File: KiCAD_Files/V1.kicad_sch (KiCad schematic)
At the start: 33 parts, among them SW1 SW_Push, SW2 SW_Push, SW3 SW_Push, U1 NodeMCU_1.0_(ESP-12E), U2 LM35-LP

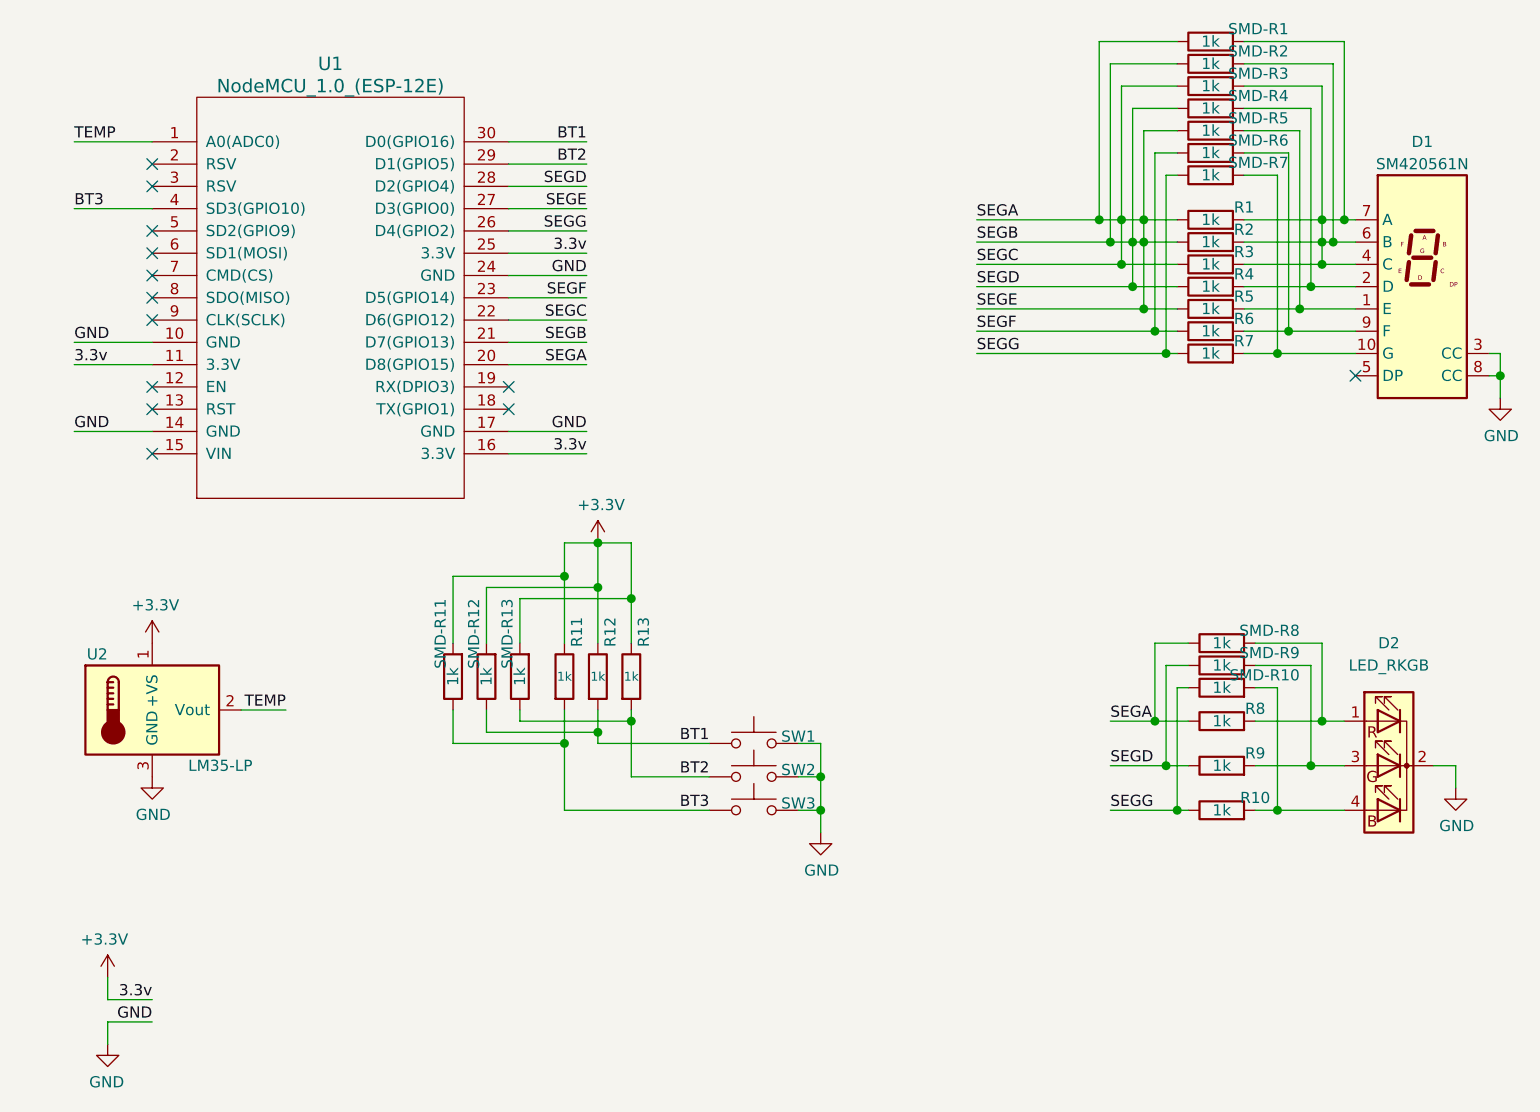
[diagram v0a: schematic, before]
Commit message: Updated Schematic. Started a Getting Started guide
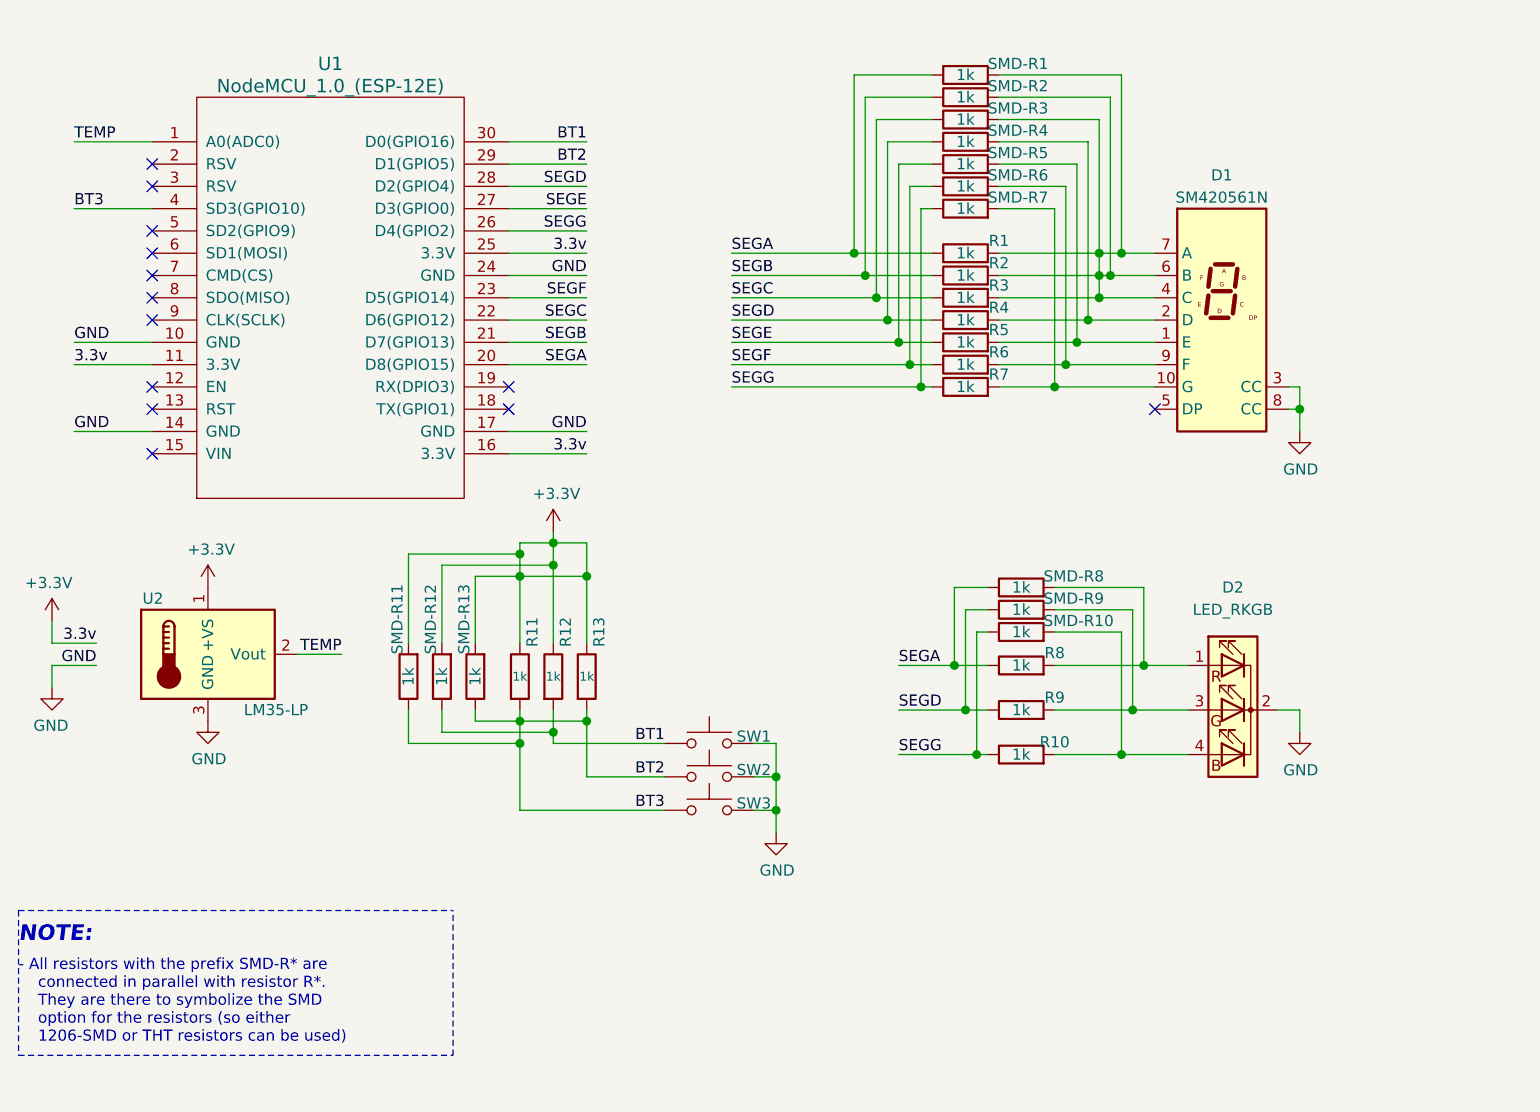
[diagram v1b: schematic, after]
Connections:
- net BT3 is gone; now on net BT2: R11.2, SMD-R11.1, SW3.1, U1.4 (SD3(GPIO10))
- net SEGA: no longer R2.1, R3.1, R4.1, R5.1, R9.1, SMD-R2.1, SMD-R3.1, SMD-R4.1, SMD-R5.1, SMD-R9.1, U1.21 (D7(GPIO13)), U1.22 (D6(GPIO12)), U1.27 (D3(GPIO0)), U1.28 (D2(GPIO4))
- new net SEGB: R2.1, SMD-R2.1, U1.21 (D7(GPIO13))
- new net SEGC: R3.1, SMD-R3.1, U1.22 (D6(GPIO12))
- new net SEGD: R4.1, R9.1, SMD-R4.1, SMD-R9.1, U1.28 (D2(GPIO4))
- new net SEGE: R5.1, SMD-R5.1, U1.27 (D3(GPIO0))
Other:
- note added: "- All resistors with the prefix SMD-R* are connected in parallel with resistor R*. They are there to symbolize the SMD option for the resistors (so either 1206-SMD or THT resistors can be used)"
- note added: "NOTE:"
- company: UNewHaven -> Electro707
- moved on the sheet: D1, D2, R1, R10, R11, R12, R13, R2, R3, R4, R5, R6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

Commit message: Added .net file. Changed origin. Last commit for V1 PCB
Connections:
- net BT2: no longer R11.2, SMD-R11.1, SW3.1, U1.4 (SD3(GPIO10))
- new net: D1.4 (C), R3.2, SMD-R3.2
- new net: D1.6 (B), R2.2, SMD-R2.2
- new net: D1.7 (A), R1.2, SMD-R1.2
- new net BT3: R11.2, SMD-R11.1, SW3.1, U1.4 (SD3(GPIO10))
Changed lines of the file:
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@@
   )
   (junction (at 71.12 77.47) (diameter 1.016) (color 0 0 0 0))
-  (junction (at 71.12 80.01) (diameter 1.016) (color 0 0 0 0))
-  (junction (at 71.12 96.52) (diameter 1.016) (color 0 0 0 0))
   (junction (at 71.12 99.06) (diameter 1.016) (color 0 0 0 0))
   (junction (at 74.93 76.2) (diameter 1.016) (color 0 0 0 0))
@@
   (junction (at 134.62 53.34) (diameter 1.016) (color 0 0 0 0))
   (junction (at 135.89 50.8) (diameter 1.016) (color 0 0 0 0))
-  (junction (at 137.16 43.18) (diameter 1.016) (color 0 0 0 0))
-  (junction (at 137.16 45.72) (diameter 1.016) (color 0 0 0 0))
   (junction (at 137.16 48.26) (diameter 1.016) (color 0 0 0 0))
   (junction (at 138.43 45.72) (diameter 1.016) (color 0 0 0 0))
@@
     (stroke (width 0) (type solid) (color 0 0 0 0))
   )
-  (wire (pts (xy 66.04 80.01) (xy 71.12 80.01))
+  (wire (pts (xy 66.04 80.01) (xy 78.74 80.01))
     (stroke (width 0) (type solid) (color 0 0 0 0))
   )
@@
     (stroke (width 0) (type solid) (color 0 0 0 0))
   )
-  (wire (pts (xy 66.04 96.52) (xy 71.12 96.52))
+  (wire (pts (xy 66.04 96.52) (xy 78.74 96.52))
     (stroke (width 0) (type solid) (color 0 0 0 0))
   )
@@
     (stroke (width 0) (type solid) (color 0 0 0 0))
   )
-  (wire (pts (xy 71.12 77.47) (xy 71.12 80.01))
-    (stroke (width 0) (type solid) (color 0 0 0 0))
-  )
-  (wire (pts (xy 71.12 80.01) (xy 71.12 87.63))
-    (stroke (width 0) (type solid) (color 0 0 0 0))
-  )
-  (wire (pts (xy 71.12 80.01) (xy 78.74 80.01))
-    (stroke (width 0) (type solid) (color 0 0 0 0))
-  )
-  (wire (pts (xy 71.12 95.25) (xy 71.12 96.52))
-    (stroke (width 0) (type solid) (color 0 0 0 0))
-  )
-  (wire (pts (xy 71.12 96.52) (xy 71.12 99.06))
-    (stroke (width 0) (type solid) (color 0 0 0 0))
-  )
-  (wire (pts (xy 71.12 96.52) (xy 78.74 96.52))
+  (wire (pts (xy 71.12 77.47) (xy 71.12 87.63))
+    (stroke (width 0) (type solid) (color 0 0 0 0))
+  )
+  (wire (pts (xy 71.12 95.25) (xy 71.12 99.06))
     (stroke (width 0) (type solid) (color 0 0 0 0))
   )
@@
     (stroke (width 0) (type solid) (color 0 0 0 0))
   )
-  (wire (pts (xy 125.73 43.18) (xy 137.16 43.18))
-    (stroke (width 0) (type solid) (color 0 0 0 0))
-  )
-  (wire (pts (xy 125.73 45.72) (xy 137.16 45.72))
+  (wire (pts (xy 125.73 43.18) (xy 139.7 43.18))
+    (stroke (width 0) (type solid) (color 0 0 0 0))
+  )
+  (wire (pts (xy 125.73 45.72) (xy 138.43 45.72))
     (stroke (width 0) (type solid) (color 0 0 0 0))
   )
@@
     (stroke (width 0) (type solid) (color 0 0 0 0))
   )
-  (wire (pts (xy 137.16 27.94) (xy 137.16 43.18))
-    (stroke (width 0) (type solid) (color 0 0 0 0))
-  )
-  (wire (pts (xy 137.16 43.18) (xy 137.16 45.72))
-    (stroke (width 0) (type solid) (color 0 0 0 0))
-  )
-  (wire (pts (xy 137.16 43.18) (xy 139.7 43.18))
-    (stroke (width 0) (type solid) (color 0 0 0 0))
-  )
-  (wire (pts (xy 137.16 45.72) (xy 137.16 48.26))
-    (stroke (width 0) (type solid) (color 0 0 0 0))
-  )
-  (wire (pts (xy 137.16 45.72) (xy 138.43 45.72))
-    (stroke (width 0) (type solid) (color 0 0 0 0))
-  )
+  (wire (pts (xy 137.16 27.94) (xy 137.16 48.26))
+    (stroke (width 0) (type solid) (color 0 0 0 0))
+  )
